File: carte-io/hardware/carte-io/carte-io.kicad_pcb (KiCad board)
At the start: 4 copper layers, 100 x 80 mm, 50 parts, among them J1 USB_C_Receptacle_USB2.0_14P, J2 JST-XH_S2B-XH-A, J3 TSW-104-07-G-T, J4 JST_PH_B4B, J5 TSW-104-07-G-T, J6 FTSH-110-01-L-DV-007, U1 STM32U545VETx, U2 FT231XQ, U3 LT1963AxST-3.3, X1 ASE-16.000MHZ-LC-T

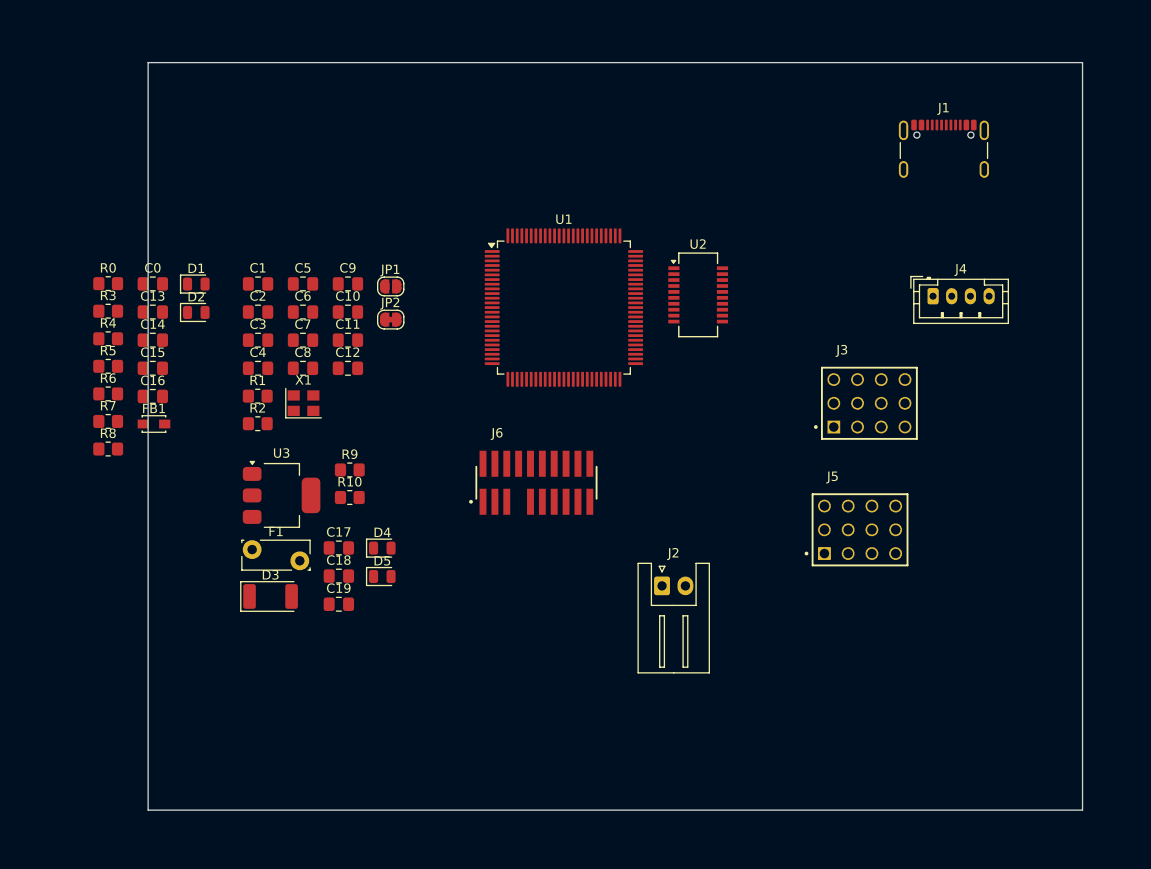
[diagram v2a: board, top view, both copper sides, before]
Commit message: Carte IO routée version 1
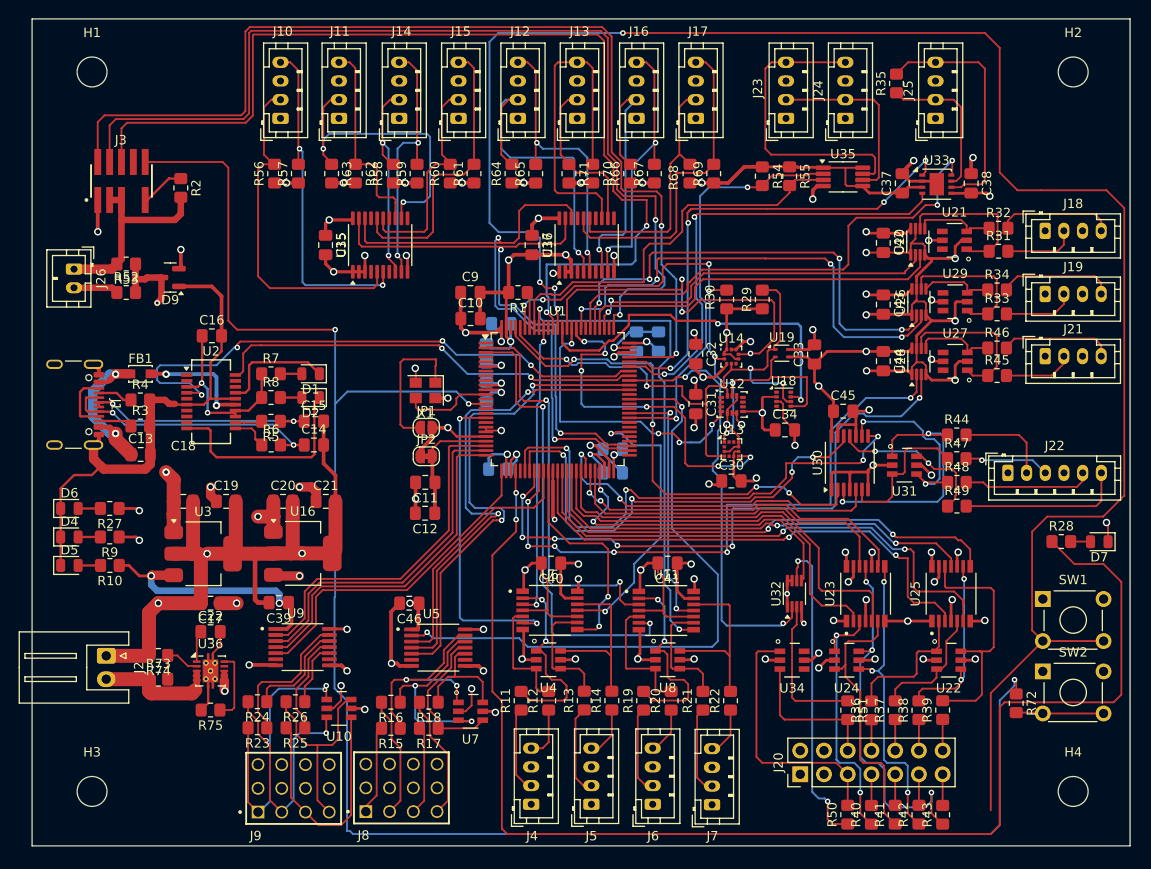
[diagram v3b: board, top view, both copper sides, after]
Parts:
- removed C0: 100nF, Capacitor_SMD:C_0805_2012Metric_Pad1.18x1.45mm_HandSolder
- removed D3: D, Diode_SMD:D_2010_5025Metric
- removed F1: Polyfuse, Fuse:Fuse_Bourns_MF-RG300
- removed R0: 100R, Resistor_SMD:R_0805_2012Metric_Pad1.20x1.40mm_HandSolder
- added C20: 100nF, Capacitor_SMD:C_0805_2012Metric_Pad1.18x1.45mm_HandSolder, F.Cu at (114.4, 107.0)
- added C21: 10µF, Capacitor_SMD:C_0805_2012Metric_Pad1.18x1.45mm_HandSolder, F.Cu at (119.0, 107.0)
- added C22: 100nF, Capacitor_SMD:C_0805_2012Metric_Pad1.18x1.45mm_HandSolder, F.Cu at (106.7, 120.9)
- added C30: 100nF, Capacitor_SMD:C_0805_2012Metric_Pad1.18x1.45mm_HandSolder, F.Cu at (162.4, 104.8)
- added C31: 100nF, Capacitor_SMD:C_0805_2012Metric_Pad1.18x1.45mm_HandSolder, F.Cu at (158.6, 96.5)
- added C32: 100nF, Capacitor_SMD:C_0805_2012Metric_Pad1.18x1.45mm_HandSolder, F.Cu at (158.6, 91.2)
- added C33: 100nF, Capacitor_SMD:C_0805_2012Metric_Pad1.18x1.45mm_HandSolder, F.Cu at (171.3, 91.2)
- added C34: 100nF, Capacitor_SMD:C_0805_2012Metric_Pad1.18x1.45mm_HandSolder, F.Cu at (168.1, 99.3)
- added C35: 100nF, Capacitor_SMD:C_0805_2012Metric_Pad1.18x1.45mm_HandSolder, F.Cu at (119.0, 79.5)
- added C36: 100nF, Capacitor_SMD:C_0805_2012Metric_Pad1.18x1.45mm_HandSolder, F.Cu at (141.1, 79.5)
- added C37: 100nF, Capacitor_SMD:C_0805_2012Metric_Pad1.18x1.45mm_HandSolder, F.Cu at (180.7, 72.9)
- added C38: 100nF, Capacitor_SMD:C_0805_2012Metric_Pad1.18x1.45mm_HandSolder, F.Cu at (188.1, 72.9)
- added C39: 100nF, Capacitor_SMD:C_0805_2012Metric_Pad1.18x1.45mm_HandSolder, F.Cu at (114.0, 117.8)
- added C40: 100nF, Capacitor_SMD:C_0805_2012Metric_Pad1.18x1.45mm_HandSolder, F.Cu at (143.1, 113.6)
- added C41: 100nF, Capacitor_SMD:C_0805_2012Metric_Pad1.18x1.45mm_HandSolder, F.Cu at (155.6, 113.6)
- added C42: 100nF, Capacitor_SMD:C_0805_2012Metric_Pad1.18x1.45mm_HandSolder, F.Cu at (178.7, 79.3)
- added C43: 100nF, Capacitor_SMD:C_0805_2012Metric_Pad1.18x1.45mm_HandSolder, F.Cu at (178.7, 85.9)
- added C44: 100nF, Capacitor_SMD:C_0805_2012Metric_Pad1.18x1.45mm_HandSolder, F.Cu at (178.7, 91.9)
- added C45: 100nF, Capacitor_SMD:C_0805_2012Metric_Pad1.18x1.45mm_HandSolder, F.Cu at (174.4, 97.3)
- added C46: 100nF, Capacitor_SMD:C_0805_2012Metric_Pad1.18x1.45mm_HandSolder, F.Cu at (128.0, 117.9)
- added D6: LED, LED_SMD:LED_0805_2012Metric, F.Cu at (91.6, 107.7)
- added D7: LED, LED_SMD:LED_0805_2012Metric, F.Cu at (201.8, 111.3)
- added D9: BAT54SFILMY, Package_TO_SOT_SMD:SOT-23, F.Cu at (102.4, 83.0)
- added H1: MountingHole, MountingHole:MountingHole_3.2mm_M3, F.Cu at (94.0, 61.0)
- added H2: MountingHole, MountingHole:MountingHole_3.2mm_M3, F.Cu at (199.0, 61.0)
- added H3: MountingHole, MountingHole:MountingHole_3.2mm_M3, F.Cu at (94.0, 138.0)
- added H4: MountingHole, MountingHole:MountingHole_3.2mm_M3, F.Cu at (199.0, 138.0)
- added J10: JST_PH_B4B, Connector_JST:JST_PH_B4B-PH-K_1x04_P2.00mm_Vertical, F.Cu at (114.2, 66.0)
- added J11: JST_PH_B4B, Connector_JST:JST_PH_B4B-PH-K_1x04_P2.00mm_Vertical, F.Cu at (120.4, 66.0)
- added J12: JST_PH_B4B, Connector_JST:JST_PH_B4B-PH-K_1x04_P2.00mm_Vertical, F.Cu at (139.6, 66.0)
- added J13: JST_PH_B4B, Connector_JST:JST_PH_B4B-PH-K_1x04_P2.00mm_Vertical, F.Cu at (145.9, 66.0)
- added J14: JST_PH_B4B, Connector_JST:JST_PH_B4B-PH-K_1x04_P2.00mm_Vertical, F.Cu at (126.9, 66.0)
- added J15: JST_PH_B4B, Connector_JST:JST_PH_B4B-PH-K_1x04_P2.00mm_Vertical, F.Cu at (133.2, 66.0)
- added J16: JST_PH_B4B, Connector_JST:JST_PH_B4B-PH-K_1x04_P2.00mm_Vertical, F.Cu at (152.3, 66.0)
- added J17: JST_PH_B4B, Connector_JST:JST_PH_B4B-PH-K_1x04_P2.00mm_Vertical, F.Cu at (158.6, 66.0)
- added J18: JST_PH_B4B, Connector_JST:JST_PH_B4B-PH-K_1x04_P2.00mm_Vertical, F.Cu at (196.0, 78.0)
- added J19: JST_PH_B4B, Connector_JST:JST_PH_B4B-PH-K_1x04_P2.00mm_Vertical, F.Cu at (196.0, 84.8)
- added J20: Conn_02x08_Odd_Even, Connector_PinHeader_2.54mm:PinHeader_2x07_P2.54mm_Vertical, F.Cu at (169.8, 136.2)
- added J21: JST_PH_B4B, Connector_JST:JST_PH_B4B-PH-K_1x04_P2.00mm_Vertical, F.Cu at (196.0, 91.4)
- added J22: JST_PH_B6B, Connector_JST:JST_PH_B6B-PH-K_1x06_P2.00mm_Vertical, F.Cu at (192.0, 103.9)
- added J23: JST_PH_B4B, Connector_JST:JST_PH_B4B-PH-K_1x04_P2.00mm_Vertical, F.Cu at (168.3, 66.0)
- added J24: JST_PH_B4B, Connector_JST:JST_PH_B4B-PH-K_1x04_P2.00mm_Vertical, F.Cu at (174.6, 66.0)
- added J25: JST_PH_B4B, Connector_JST:JST_PH_B4B-PH-K_1x04_P2.00mm_Vertical, F.Cu at (184.3, 66.0)
- added J26: JST-PH-B2B, Connector_JST:JST_PH_B2B-PH-K_1x02_P2.00mm_Vertical, F.Cu at (92.1, 82.1)
- added J7: JST_PH_B4B, Connector_JST:JST_PH_B4B-PH-K_1x04_P2.00mm_Vertical, F.Cu at (160.3, 139.4)
- added J8: TSW-104-07-G-T, TSW-104-07-G-T:SAMTEC_TSW-104-07-G-T, F.Cu at (127.1, 137.6)
- added J9: TSW-104-07-G-T, TSW-104-07-G-T:SAMTEC_TSW-104-07-G-T, F.Cu at (115.6, 137.7)
- added R11: 100R, Resistor_SMD:R_0805_2012Metric_Pad1.20x1.40mm_HandSolder, F.Cu at (139.9, 128.3)
- added R12: 100R, Resistor_SMD:R_0805_2012Metric_Pad1.20x1.40mm_HandSolder, F.Cu at (142.9, 128.3)
- added R13: 100R, Resistor_SMD:R_0805_2012Metric_Pad1.20x1.40mm_HandSolder, F.Cu at (146.7, 128.3)
- added R14: 100R, Resistor_SMD:R_0805_2012Metric_Pad1.20x1.40mm_HandSolder, F.Cu at (149.6, 128.3)
- added R15: 100R, Resistor_SMD:R_0805_2012Metric_Pad1.20x1.40mm_HandSolder, F.Cu at (126.0, 131.2)
- added R16: 100R, Resistor_SMD:R_0805_2012Metric_Pad1.20x1.40mm_HandSolder, F.Cu at (126.0, 128.5)
- added R17: 100R, Resistor_SMD:R_0805_2012Metric_Pad1.20x1.40mm_HandSolder, F.Cu at (130.0, 131.2)
- added R18: 100R, Resistor_SMD:R_0805_2012Metric_Pad1.20x1.40mm_HandSolder, F.Cu at (130.0, 128.5)
- added R19: 100R, Resistor_SMD:R_0805_2012Metric_Pad1.20x1.40mm_HandSolder, F.Cu at (153.0, 128.3)
- added R20: 100R, Resistor_SMD:R_0805_2012Metric_Pad1.20x1.40mm_HandSolder, F.Cu at (156.0, 128.3)
- added R21: 100R, Resistor_SMD:R_0805_2012Metric_Pad1.20x1.40mm_HandSolder, F.Cu at (159.4, 128.3)
- added R22: 100R, Resistor_SMD:R_0805_2012Metric_Pad1.20x1.40mm_HandSolder, F.Cu at (162.3, 128.3)
- added R23: 100R, Resistor_SMD:R_0805_2012Metric_Pad1.20x1.40mm_HandSolder, F.Cu at (111.7, 131.2)
- added R24: 100R, Resistor_SMD:R_0805_2012Metric_Pad1.20x1.40mm_HandSolder, F.Cu at (111.7, 128.4)
- added R25: 100R, Resistor_SMD:R_0805_2012Metric_Pad1.20x1.40mm_HandSolder, F.Cu at (115.8, 131.2)
- added R26: 100R, Resistor_SMD:R_0805_2012Metric_Pad1.20x1.40mm_HandSolder, F.Cu at (115.8, 128.4)
- added R27: 100R, Resistor_SMD:R_0805_2012Metric_Pad1.20x1.40mm_HandSolder, F.Cu at (95.9, 107.7)
- added R28: 1K, Resistor_SMD:R_0805_2012Metric_Pad1.20x1.40mm_HandSolder, F.Cu at (197.7, 111.3)
- added R29: 1K, Resistor_SMD:R_0805_2012Metric_Pad1.20x1.40mm_HandSolder, F.Cu at (165.7, 85.3)
- added R30: 1K, Resistor_SMD:R_0805_2012Metric_Pad1.20x1.40mm_HandSolder, F.Cu at (161.9, 85.3)
- added R31: 100R, Resistor_SMD:R_0805_2012Metric_Pad1.20x1.40mm_HandSolder, F.Cu at (191.0, 80.2)
- added R32: 100R, Resistor_SMD:R_0805_2012Metric_Pad1.20x1.40mm_HandSolder, F.Cu at (191.0, 77.7)
- added R33: 100R, Resistor_SMD:R_0805_2012Metric_Pad1.20x1.40mm_HandSolder, F.Cu at (190.9, 86.9)
- added R34: 100R, Resistor_SMD:R_0805_2012Metric_Pad1.20x1.40mm_HandSolder, F.Cu at (190.9, 84.3)
- added R35: 120R, Resistor_SMD:R_0805_2012Metric_Pad1.20x1.40mm_HandSolder, F.Cu at (180.1, 62.2)
- added R36: 100R, Resistor_SMD:R_0805_2012Metric_Pad1.20x1.40mm_HandSolder, F.Cu at (177.4, 129.3)
- added R37: 100R, Resistor_SMD:R_0805_2012Metric_Pad1.20x1.40mm_HandSolder, F.Cu at (179.9, 129.3)
- added R38: 100R, Resistor_SMD:R_0805_2012Metric_Pad1.20x1.40mm_HandSolder, F.Cu at (182.5, 129.3)
- added R39: 100R, Resistor_SMD:R_0805_2012Metric_Pad1.20x1.40mm_HandSolder, F.Cu at (185.0, 129.3)
- added R40: 100R, Resistor_SMD:R_0805_2012Metric_Pad1.20x1.40mm_HandSolder, F.Cu at (177.4, 140.5)
- added R41: 100R, Resistor_SMD:R_0805_2012Metric_Pad1.20x1.40mm_HandSolder, F.Cu at (179.9, 140.5)
- added R42: 100R, Resistor_SMD:R_0805_2012Metric_Pad1.20x1.40mm_HandSolder, F.Cu at (182.5, 140.5)
- added R43: 100R, Resistor_SMD:R_0805_2012Metric_Pad1.20x1.40mm_HandSolder, F.Cu at (185.0, 140.5)
- added R44: 100R, Resistor_SMD:R_0805_2012Metric_Pad1.20x1.40mm_HandSolder, F.Cu at (186.5, 99.8)
- added R45: 100R, Resistor_SMD:R_0805_2012Metric_Pad1.20x1.40mm_HandSolder, F.Cu at (190.9, 93.5)
- added R46: 100R, Resistor_SMD:R_0805_2012Metric_Pad1.20x1.40mm_HandSolder, F.Cu at (190.9, 90.5)
- added R47: 100R, Resistor_SMD:R_0805_2012Metric_Pad1.20x1.40mm_HandSolder, F.Cu at (186.5, 102.4)
- added R48: 100R, Resistor_SMD:R_0805_2012Metric_Pad1.20x1.40mm_HandSolder, F.Cu at (186.6, 104.9)
- added R49: 100R, Resistor_SMD:R_0805_2012Metric_Pad1.20x1.40mm_HandSolder, F.Cu at (186.6, 107.5)
- added R50: 100R, Resistor_SMD:R_0805_2012Metric_Pad1.20x1.40mm_HandSolder, F.Cu at (174.9, 140.5)
- added R51: 100R, Resistor_SMD:R_0805_2012Metric_Pad1.20x1.40mm_HandSolder, F.Cu at (174.9, 129.3)
- added R52: 100R, Resistor_SMD:R_0805_2012Metric_Pad1.20x1.40mm_HandSolder, F.Cu at (97.7, 84.6)
- added R53: 100R, Resistor_SMD:R_0805_2012Metric_Pad1.20x1.40mm_HandSolder, F.Cu at (97.7, 81.6)
- added R54: 1K, Resistor_SMD:R_0805_2012Metric_Pad1.20x1.40mm_HandSolder, F.Cu at (165.7, 72.2)
- added R55: 1K, Resistor_SMD:R_0805_2012Metric_Pad1.20x1.40mm_HandSolder, F.Cu at (168.7, 72.2)
- added R56: 1K, Resistor_SMD:R_0805_2012Metric_Pad1.20x1.40mm_HandSolder, F.Cu at (113.5, 71.9)
- added R57: 1K, Resistor_SMD:R_0805_2012Metric_Pad1.20x1.40mm_HandSolder, F.Cu at (116.1, 71.9)
- added R58: 1K, Resistor_SMD:R_0805_2012Metric_Pad1.20x1.40mm_HandSolder, F.Cu at (126.2, 71.9)
- added R59: 1K, Resistor_SMD:R_0805_2012Metric_Pad1.20x1.40mm_HandSolder, F.Cu at (128.8, 71.9)
- added R60: 1K, Resistor_SMD:R_0805_2012Metric_Pad1.20x1.40mm_HandSolder, F.Cu at (132.3, 71.9)
- added R61: 1K, Resistor_SMD:R_0805_2012Metric_Pad1.20x1.40mm_HandSolder, F.Cu at (134.9, 71.9)
- added R62: 1K, Resistor_SMD:R_0805_2012Metric_Pad1.20x1.40mm_HandSolder, F.Cu at (122.2, 71.9)
- added R63: 1K, Resistor_SMD:R_0805_2012Metric_Pad1.20x1.40mm_HandSolder, F.Cu at (119.6, 71.9)
- added R64: 1K, Resistor_SMD:R_0805_2012Metric_Pad1.20x1.40mm_HandSolder, F.Cu at (138.9, 71.9)
- added R65: 1K, Resistor_SMD:R_0805_2012Metric_Pad1.20x1.40mm_HandSolder, F.Cu at (141.5, 71.9)
- added R66: 1K, Resistor_SMD:R_0805_2012Metric_Pad1.20x1.40mm_HandSolder, F.Cu at (151.6, 71.9)
- added R67: 1K, Resistor_SMD:R_0805_2012Metric_Pad1.20x1.40mm_HandSolder, F.Cu at (154.2, 71.9)
- added R68: 1K, Resistor_SMD:R_0805_2012Metric_Pad1.20x1.40mm_HandSolder, F.Cu at (158.0, 71.9)
- added R69: 1K, Resistor_SMD:R_0805_2012Metric_Pad1.20x1.40mm_HandSolder, F.Cu at (160.5, 71.9)
- added R70: 1K, Resistor_SMD:R_0805_2012Metric_Pad1.20x1.40mm_HandSolder, F.Cu at (147.6, 71.9)
- added R71: 1K, Resistor_SMD:R_0805_2012Metric_Pad1.20x1.40mm_HandSolder, F.Cu at (145.0, 71.9)
- added R72: 10K, Resistor_SMD:R_0805_2012Metric_Pad1.20x1.40mm_HandSolder, F.Cu at (192.9, 128.6)
- added R73: 5.1K, Resistor_SMD:R_0805_2012Metric_Pad1.20x1.40mm_HandSolder, F.Cu at (101.1, 126.0)
- added R74: 5.1K, Resistor_SMD:R_0805_2012Metric_Pad1.20x1.40mm_HandSolder, F.Cu at (101.1, 123.4)
- added R75: 5.1K, Resistor_SMD:R_0805_2012Metric_Pad1.20x1.40mm_HandSolder, F.Cu at (106.7, 129.3)
- added SW1: SW_Push, Button_Switch_THT:SW_TH_Tactile_Omron_B3F-10xx, F.Cu at (195.8, 117.4)
- added SW2: SW_Push, Button_Switch_THT:SW_TH_Tactile_Omron_B3F-10xx, F.Cu at (195.8, 125.2)
- added U10: CM1293A-04SO, CM1293A-04SO:SOT95P285X140-6N, F.Cu at (120.4, 129.1)
- added U11: 74LVC125APW, 74LVC125APW:IC_74LVC125APW, F.Cu at (155.4, 118.6)
- added U12: LSM6DS3, Package_LGA:LGA-14_3x2.5mm_P0.5mm_LayoutBorder3x4y, F.Cu at (162.5, 96.6)
- added U13: LIS2MDL, Package_LGA:LGA-12_2x2mm_P0.5mm, F.Cu at (162.4, 101.4)
- added U14: LPS22DF, Package_LGA:ST_HLGA-10_2x2mm_P0.5mm_LayoutBorder3x2y, F.Cu at (162.4, 91.5)
- added U15: PCA9544APW, Package_SO:TSSOP-20_4.4x6.5mm_P0.65mm, F.Cu at (124.8, 79.5)
- added U16: LT1963AxST-3.3, Package_TO_SOT_SMD:SOT-223-3_TabPin2, F.Cu at (116.6, 112.5)
- added U17: PCA9544APW, Package_SO:TSSOP-20_4.4x6.5mm_P0.65mm, F.Cu at (146.9, 79.5)
- added U18: APDS-9251-001, OptoDevice:Broadcom_LGA-8_2x2mm_P0.5mm, F.Cu at (168.0, 96.0)
- added U19: SHT4x, Sensor_Humidity:Sensirion_DFN-4_1.5x1.5mm_P0.8mm_SHT4x_NoCentralPad, F.Cu at (167.8, 91.1)
- added U20: 74LVC2G125DP,125, Package_SO:VSSOP-8_2.3x2mm_P0.5mm, F.Cu at (182.4, 79.2)
- added U21: CM1293A-04SO, CM1293A-04SO:SOT95P285X140-6N, F.Cu at (186.3, 79.0)
- added U22: CM1293A-04SO, CM1293A-04SO:SOT95P285X140-6N, F.Cu at (185.7, 124.0)
- added U23: 74LVC125APW, 74LVC125APW:IC_74LVC125APW, F.Cu at (176.8, 116.8)
- added U24: CM1293A-04SO, CM1293A-04SO:SOT95P285X140-6N, F.Cu at (174.8, 124.0)
- added U25: 74LVC125APW, 74LVC125APW:IC_74LVC125APW, F.Cu at (185.9, 116.8)
- added U26: 74LVC2G125DP,125, Package_SO:VSSOP-8_2.3x2mm_P0.5mm, F.Cu at (182.5, 85.6)
- added U27: CM1293A-04SO, CM1293A-04SO:SOT95P285X140-6N, F.Cu at (186.4, 92.0)
- added U28: 74LVC2G125DP,125, Package_SO:VSSOP-8_2.3x2mm_P0.5mm, F.Cu at (182.5, 92.0)
- added U29: CM1293A-04SO, CM1293A-04SO:SOT95P285X140-6N, F.Cu at (186.4, 85.6)
- added U30: 74LVC125APW,118, Package_SO:TSSOP-14_4.4x5mm_P0.65mm, F.Cu at (175.1, 102.8)
- added U31: CM1293A-04SO, CM1293A-04SO:SOT95P285X140-6N, F.Cu at (180.9, 103.1)
- added U32: 74LVC2G125DP,125, Package_SO:VSSOP-8_2.3x2mm_P0.5mm, F.Cu at (169.2, 116.8)
- added U33: MCP2542FDxMF, Package_DFN_QFN:DFN-8-1EP_3x3mm_P0.65mm_EP1.55x2.4mm, F.Cu at (184.4, 73.0)
- added U34: CM1293A-04SO, CM1293A-04SO:SOT95P285X140-6N, F.Cu at (168.9, 124.0)
- added U35: TCA9802, Package_SO:VSSOP-8_3x3mm_P0.65mm, F.Cu at (174.4, 72.2)
- added U36: TPS259250DRCT, Package_SON:VSON-10-1EP_3x3mm_P0.5mm_EP1.65x2.4mm_ThermalVias, F.Cu at (106.7, 125.1)
- added U4: CM1293A-04SO, CM1293A-04SO:SOT95P285X140-6N, F.Cu at (142.8, 123.9)
- added U5: TXU0104PWR, TXU0104PWR:SOP65P640X120-14N, F.Cu at (131.1, 122.6)
- added U6: 74LVC125APW, 74LVC125APW:IC_74LVC125APW, F.Cu at (143.0, 118.6)
- added U7: CM1293A-04SO, CM1293A-04SO:SOT95P285X140-6N, F.Cu at (134.5, 129.4)
- added U8: CM1293A-04SO, CM1293A-04SO:SOT95P285X140-6N, F.Cu at (155.6, 123.9)
- added U9: TXU0104PWR, TXU0104PWR:SOP65P640X120-14N, F.Cu at (116.5, 122.6)
- C1, C2, C3, C4, C5, C6, C7, C8: moved to B.Cu
- C14: value 10nf -> 47pF
- C16: value 47pF -> 10nf
- C17, C19: value 100nF -> 10µF
- J3: value TSW-104-07-G-T -> FTSH-105-01-L-DV-007; footprint TSW-104-07-G-T:SAMTEC_TSW-104-07-G-T -> FTSH-105-01-L-DV-007-K:SAMTEC_FTSH-105-X-X-DV-007-P-X
- J5: value TSW-104-07-G-T -> JST_PH_B4B; footprint TSW-104-07-G-T:SAMTEC_TSW-104-07-G-T -> Connector_JST:JST_PH_B4B-PH-K_1x04_P2.00mm_Vertical
- J6: value FTSH-110-01-L-DV-007 -> JST_PH_B4B; footprint FTSH-110-01-L-DV-007:SAMTEC_FTSH-110-01-L-DV-007 -> Connector_JST:JST_PH_B4B-PH-K_1x04_P2.00mm_Vertical
- R2: value 100R -> 10K
- R5, R6: value 100R -> 27R
- R7, R8: value 27R -> 1K
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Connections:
- net /CPU/LPUART1_RX renamed /CPU/COM_EXT_RX
- net /CPU/SPI2_MOSI renamed /CPU/US_PulseStart
- net Net-(U2-VCC) renamed /Power & Analog/FT231_VCC
- C14 pad 1: Net-(U2-3V3OUT) -> /Power & Analog/USB-DP
- C15 pad 1: Net-(C15-Pad1) -> /Power & Analog/USB-DN
- C16 pad 1: Net-(C16-Pad1) -> Net-(U2-3V3OUT)
- J1 pad A6: Net-(C16-Pad1) -> /Power & Analog/USB-DN
- J1 pad A7: Net-(C16-Pad1) -> /Power & Analog/USB-DN
- J1 pad B6: Net-(C15-Pad1) -> /Power & Analog/USB-DP
- J1 pad B7: Net-(C15-Pad1) -> /Power & Analog/USB-DP
- J2 pad 2: Net-(J2-Pin_2) -> /Power & Analog/VIN
- J3 pad 01: unconnected-(J3-Pad01) -> +3.3V
- J3 pad 02: unconnected-(J3-Pad02) -> /CPU/JTMS-SWDIO
- J3 pad 03: unconnected-(J3-Pad03) -> GND
- J3 pad 04: unconnected-(J3-Pad04) -> /CPU/JTCK-SWCLK
- J3 pad 05: unconnected-(J3-Pad05) -> GND
- J3 pad 06: unconnected-(J3-Pad06) -> /CPU/JTDO-SWO
- J3 pad 09: unconnected-(J3-Pad09) -> /CPU/GNDDetect
- J3 pad 10: unconnected-(J3-Pad10) -> /CPU/NRST
- J4 pad 1: unconnected-(J4-Pin_1-Pad1) -> +3.3V
- J4 pad 2: unconnected-(J4-Pin_2-Pad2) -> Net-(J4-Pin_2)
- J4 pad 3: unconnected-(J4-Pin_3-Pad3) -> GND
- J4 pad 4: unconnected-(J4-Pin_4-Pad4) -> Net-(J4-Pin_4)
- R5 pad 1: Net-(U2-3V3OUT) -> /Power & Analog/USB-DN
- R5 pad 2: Net-(D1-A) -> /Power & Analog/USB2-DN
- R6 pad 1: Net-(U2-3V3OUT) -> /Power & Analog/USB2-DP
- R6 pad 2: Net-(D2-A) -> /Power & Analog/USB-DP
- R7 pad 1: Net-(C16-Pad1) -> Net-(U2-3V3OUT)
- R7 pad 2: Net-(U2-USBDM) -> Net-(D1-A)
- R8 pad 1: Net-(U2-USBDP) -> Net-(U2-3V3OUT)
- R8 pad 2: Net-(C15-Pad1) -> Net-(D2-A)
- U1 pad 17: /CPU/SPI2_MISO -> /CPU/ENCODER_1_PHB
- U1 pad 29: /CPU/US_PWM -> /CPU/LED_ACTIVITY
- U1 pad 32: /CPU/I2C3_SCL -> /CPU/SPI_MOSI
- U1 pad 36: unconnected-(U1-PB1-Pad36) -> /CPU/ENCODER_2_PHA
- U1 pad 38: unconnected-(U1-PE7-Pad38) -> /CPU/INPUT1
- U1 pad 39: unconnected-(U1-PE8-Pad39) -> /CPU/INPUT2
- U1 pad 4: unconnected-(U1-PE5-Pad4) -> /CPU/~{POWEROFF}
- U1 pad 40: /CPU/ENCODER_1_PHA -> /CPU/INPUT3
- U1 pad 41: unconnected-(U1-PE10-Pad41) -> /CPU/INPUT4
- U1 pad 42: /CPU/ENCODER_1_PHB -> /CPU/OUTPUT1
- U1 pad 43: unconnected-(U1-PE12-Pad43) -> /CPU/OUTPUT2
- U1 pad 45: unconnected-(U1-PE14-Pad45) -> /CPU/OUTPUT3
- U1 pad 46: /CPU/SPI_MOSI -> /CPU/OUTPUT4
- U1 pad 47: /CPU/ENCODER_2_PHB -> /CPU/GEN_PWM2
- U1 pad 52: /CPU/SPI2_SCK -> /CPU/I2C_SCL_EXTERNAL
- U1 pad 53: /CPU/GEN_PWM1 -> /CPU/I2C_SDA_EXTERNAL
- U1 pad 54: /CPU/GEN_PWM2 -> unconnected-(U1-PB15-Pad54)
- U1 pad 56: unconnected-(U1-PD9-Pad56) -> /CPU/ENCODER_2_PHB
- U1 pad 59: /CPU/ENCODER_4_PHA -> /CPU/I2C_SCL_ARBITRARY
- U1 pad 62: unconnected-(U1-PD15-Pad62) -> /CPU/US_PulseEnd
- U1 pad 67: unconnected-(U1-PA8-Pad67) -> /CPU/GEN_PWM1
- U1 pad 77: /CPU/ENCODER_2_PHA -> unconnected-(U1-PA15-Pad77)
- U1 pad 81: unconnected-(U1-PD0-Pad81) -> /CPU/FDCAN_STBY
- U1 pad 84: unconnected-(U1-PD3-Pad84) -> /CPU/INT_MAGNETO
- U1 pad 85: unconnected-(U1-PD4-Pad85) -> /CPU/INT_IMU
- U1 pad 86: unconnected-(U1-PD5-Pad86) -> /CPU/INT_PRESSURE
- U1 pad 87: unconnected-(U1-PD6-Pad87) -> /CPU/INT_LIGHT
- U1 pad 88: unconnected-(U1-PD7-Pad88) -> /CPU/USER_BTN
- U1 pad 90: /CPU/I2C_SDA_EXT -> unconnected-(U1-PB4-Pad90)
- U1 pad 91: unconnected-(U1-PB5-Pad91) -> /CPU/ENCODER_1_PHA
- U1 pad 92: /CPU/I2C_SCL_INT -> /CPU/ENCODER_4_PHA
- U1 pad 93: /CPU/I2C_SDA_EXT -> /CPU/I2C_SDA_ARBITRARY
- U1 pad 95: unconnected-(U1-PB8-Pad95) -> /CPU/I2C_SCL_INT
- U1 pad 96: unconnected-(U1-PB9-Pad96) -> /CPU/I2C_SDA_INT
- U1 pad 97: unconnected-(U1-PE0-Pad97) -> /CPU/SPI_CS
- U2 pad 11: Net-(U2-USBDP) -> /Power & Analog/USB2-DP
- U2 pad 12: Net-(U2-USBDM) -> /Power & Analog/USB2-DN
- U2 pad 20: /IO/USB_UART_TX -> /CPU/COM_USB_TX
- U2 pad 4: /IO/USB_UART_RX -> /CPU/COM_USB_RX
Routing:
- net GND: track 0.00 -> 440.0 mm, vias 0 -> 59
- net +3.3V: track 0.00 -> 319.9 mm, vias 0 -> 53
- net /CPU/USER_BTN: track 0.00 -> 201.6 mm, vias 0 -> 4
- net /CPU/NRST: track 0.00 -> 197.0 mm, vias 0 -> 3
- net +3.3V_PWR: track 0.00 -> 191.5 mm, vias 0 -> 3
- net +5V: track 0.00 -> 180.5 mm, vias 0 -> 9
- net /CPU/LED_ACTIVITY: track 0.00 -> 141.2 mm, vias 0 -> 2
- net /CPU/JTMS-SWDIO: track 0.00 -> 112.9 mm, vias 0 -> 2
- net /CPU/JTDO-SWO: track 0.00 -> 109.0 mm, vias 0 -> 2
- net /CPU/JTCK-SWCLK: track 0.00 -> 106.9 mm, vias 0 -> 2
- net /CPU/ADC_VBAT: track 0.00 -> 76.3 mm, vias 0 -> 2
- net /CPU/SERVO_PWM1: track 0.00 -> 67.3 mm, vias 0 -> 2
- net /CPU/COM_GPS_RX: track 0.00 -> 67.1 mm, vias 0 -> 6
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- added copper zone on In2.Cu, net +3.3V
- added copper zone on In2.Cu, net +3.3V_PWR
- added copper zone on In2.Cu, net +5V
- added copper zone on In1.Cu, net GND
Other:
- board size 100 x 80 mm -> 117.5 x 88.5 mm

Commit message: Correction de DRC et modifications cosmetiques
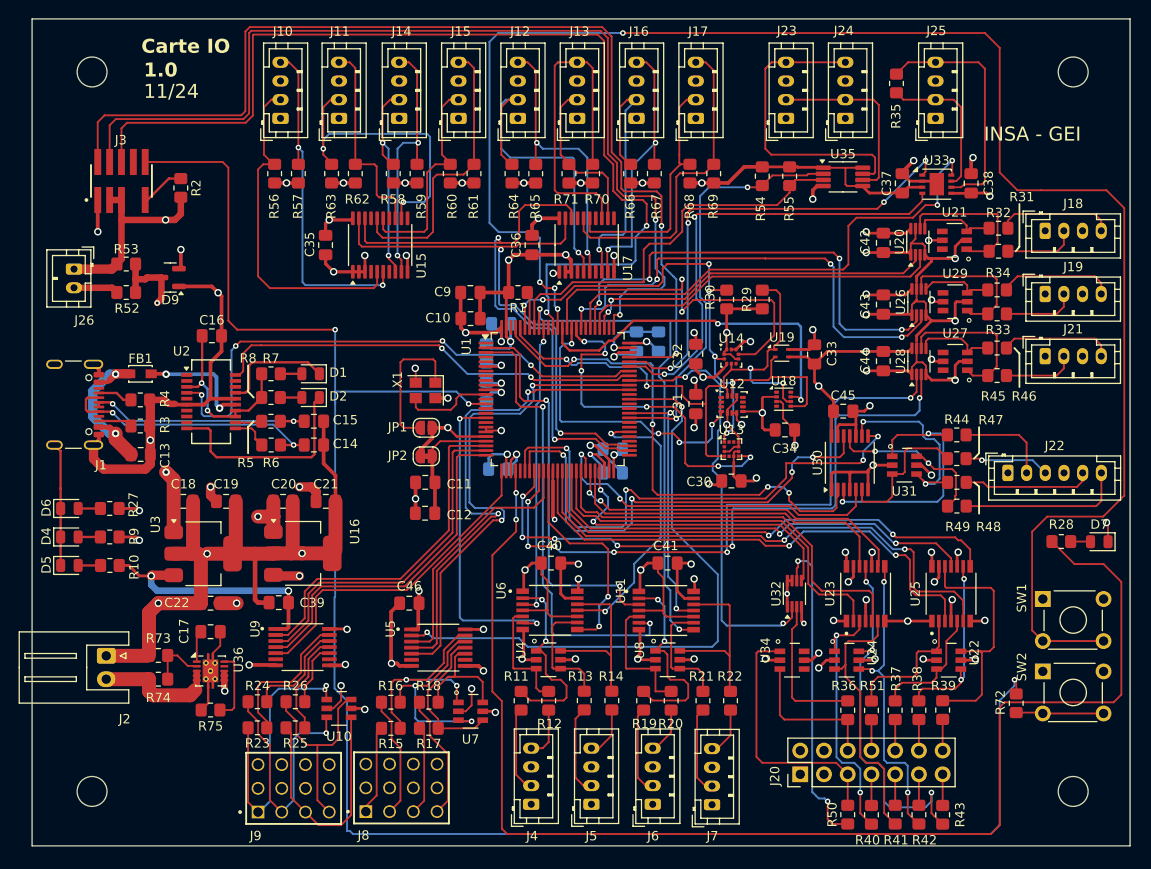
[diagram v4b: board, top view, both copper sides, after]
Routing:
- net /CPU/USER_BTN: track 201.6 -> 181.2 mm
- net (no net): track 6.77 -> 0.00 mm
- net /CPU/COM_USB_RX: track 62.1 -> 58.7 mm
- net +3.3V: track 319.9 -> 322.4 mm
- net /CPU/SPI_CS: track 53.0 -> 54.8 mm
- net /CPU/COM_GPS_RX: track 67.1 -> 68.6 mm
- net /CPU/COM_GPS_TX: track 66.9 -> 68.3 mm
- net /CPU/SPI_MOSI: track 49.9 -> 51.3 mm
- net /CPU/INT_LIGHT: track 39.3 -> 38.2 mm
- net /CPU/COM_LIDAR1_TX: track 39.2 -> 38.2 mm
- net /CPU/COM_LIDAR1_RX: track 40.0 -> 39.2 mm
- net /CPU/INPUT1: track 54.4 -> 55.2 mm
- net /CPU/NRST: track 197.0 -> 197.8 mm
- net /CPU/OUTPUT2: track 44.8 -> 44.1 mm
- net /CPU/GEN_PWM2: track 34.5 -> 33.7 mm
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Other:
- board text added: "1.0"
- board text added: "11/24"
- board text added: "Carte IO"
- board text added: "INSA - GEI"

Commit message: Correction du 5V sur les UART (Lidar et GPS + Changement de conencteur J27 (GPS) pour rajouter le 5V et le 3V pour les IO
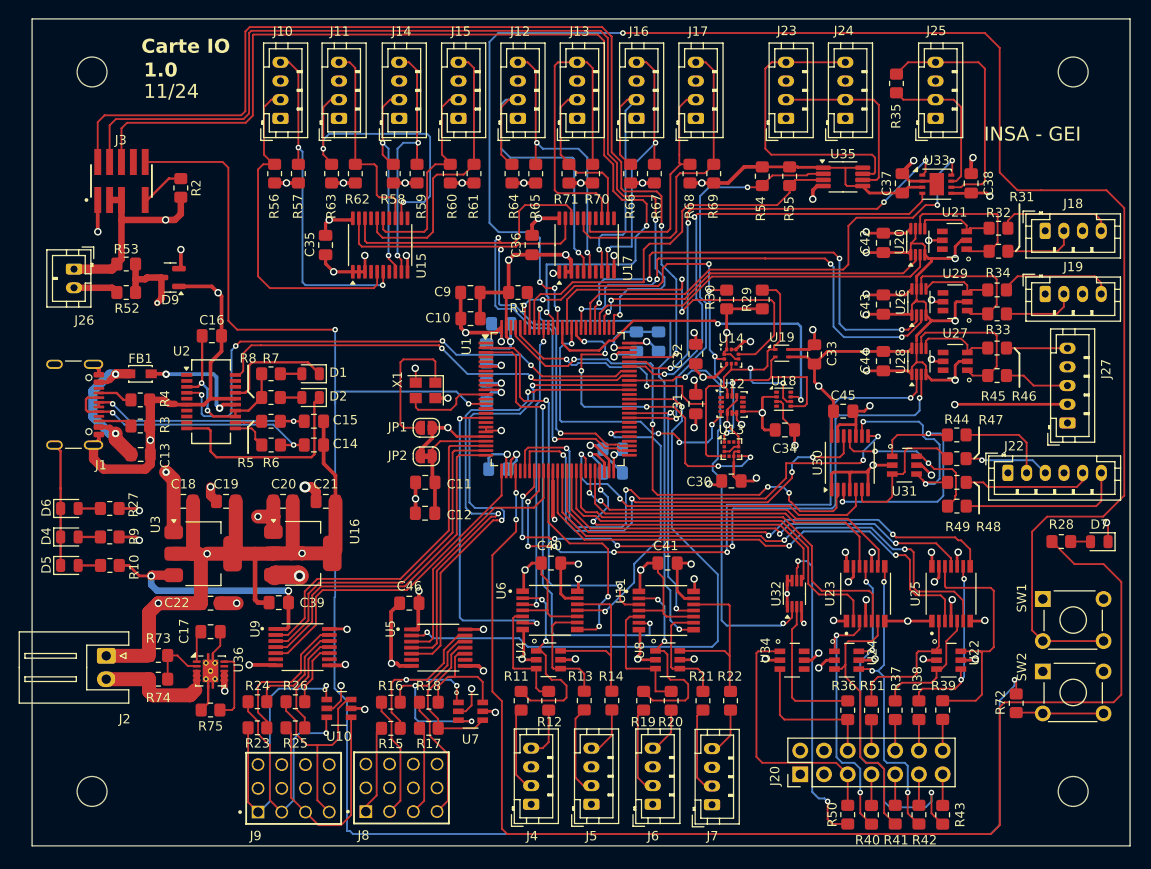
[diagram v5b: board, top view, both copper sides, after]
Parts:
- removed J21: JST_PH_B4B, Connector_JST:JST_PH_B4B-PH-K_1x04_P2.00mm_Vertical
- added J27: JST_PH_B5B, Connector_JST:JST_PH_B5B-PH-K_1x05_P2.00mm_Vertical, F.Cu at (198.4, 98.6)
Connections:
- J18 pad 1: +3.3V_PWR -> +5V
- J19 pad 1: +3.3V_PWR -> +5V
- U21 pad 5: +3.3V -> +5V
- U27 pad 5: +3.3V -> +5V
- U29 pad 5: +3.3V -> +5V
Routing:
- net +5V: track 180.5 -> 225.4 mm, vias 9 -> 12
- net +3.3V: track 322.4 -> 330.3 mm, vias 53 -> 51
- net Net-(J27-Pin_5): track 12.1 -> 6.69 mm
- net Net-(J27-Pin_3): track 7.77 -> 6.98 mm

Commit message: Carte version 1.1 terminée
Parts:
- removed C17: 10µF, Capacitor_SMD:C_0805_2012Metric_Pad1.18x1.45mm_HandSolder
- removed C22, C39, C40, C41, C46: 100nF, Capacitor_SMD:C_0805_2012Metric_Pad1.18x1.45mm_HandSolder
- removed R38, R39, R44, R47, R48, R49, R50, R51: 100R, Resistor_SMD:R_0805_2012Metric_Pad1.20x1.40mm_HandSolder
- removed R75: 5.1K, Resistor_SMD:R_0805_2012Metric_Pad1.20x1.40mm_HandSolder
- removed U22, U31, U34: CM1293A-04SO, CM1293A-04SO:SOT95P285X140-6N
- removed U23, U25: 74LVC125APW, 74LVC125APW:IC_74LVC125APW
- removed U30: 74LVC125APW,118, Package_SO:TSSOP-14_4.4x5mm_P0.65mm
- removed U32: 74LVC2G125DP,125, Package_SO:VSSOP-8_2.3x2mm_P0.5mm
- removed U36: TPS259250DRCT, Package_SON:VSON-10-1EP_3x3mm_P0.5mm_EP1.65x2.4mm_ThermalVias
- added D3: BAT54SFILMY, Package_TO_SOT_SMD:SOT-23, F.Cu at (185.7, 108.7)
- added D8: BAT54SFILMY, Package_TO_SOT_SMD:SOT-23, B.Cu at (185.7, 102.6)
- added J21: 114020164, SeeedStudio - Horizontal Header -114020164:SEEEDSTUDIO_114020164, B.Cu at (172.4, 138.2)
- added J28: 114020164, SeeedStudio - Horizontal Header -114020164:SEEEDSTUDIO_114020164, B.Cu at (185.4, 138.2)
- added J29: 114020164, SeeedStudio - Horizontal Header -114020164:SEEEDSTUDIO_114020164, F.Cu at (199.3, 105.5)
- added J30: 114020164, SeeedStudio - Horizontal Header -114020164:SEEEDSTUDIO_114020164, B.Cu at (199.3, 105.5)
- added JP3: Jumper_2_Bridged, Connector_PinHeader_2.54mm:PinHeader_1x02_P2.54mm_Horizontal, F.Cu at (105.4, 133.5)
- added Q1: IRF9388TRPBF, Package_SO:SOIC-8_3.9x4.9mm_P1.27mm, F.Cu at (103.8, 122.0)
- added R76: 4.7K, Resistor_SMD:R_0805_2012Metric_Pad1.20x1.40mm_HandSolder, F.Cu at (134.2, 78.1)
- added R77: 4.7K, Resistor_SMD:R_0805_2012Metric_Pad1.20x1.40mm_HandSolder, F.Cu at (134.2, 81.0)
- C1: moved to F.Cu
- C33, D9, R13, R14, R21, R22, R37, R41, R42, R52, R53: moved to B.Cu
- J10, J16, J18, J23, J25, J4, J6: value JST_PH_B4B -> 114020164; footprint Connector_JST:JST_PH_B4B-PH-K_1x04_P2.00mm_Vertical -> SeeedStudio - Horizontal Header -114020164:SEEEDSTUDIO_114020164
- J11, J17, J19, J24, J5, J7: value JST_PH_B4B -> 114020164; footprint Connector_JST:JST_PH_B4B-PH-K_1x04_P2.00mm_Vertical -> SeeedStudio - Horizontal Header -114020164:SEEEDSTUDIO_114020164; moved to B.Cu
- J12: renamed from J14; value JST_PH_B4B -> 114020164; footprint Connector_JST:JST_PH_B4B-PH-K_1x04_P2.00mm_Vertical -> SeeedStudio - Horizontal Header -114020164:SEEEDSTUDIO_114020164
- J13: renamed from J15; value JST_PH_B4B -> 114020164; footprint Connector_JST:JST_PH_B4B-PH-K_1x04_P2.00mm_Vertical -> SeeedStudio - Horizontal Header -114020164:SEEEDSTUDIO_114020164; moved to B.Cu
- J14: renamed from J12; value JST_PH_B4B -> 114020164; footprint Connector_JST:JST_PH_B4B-PH-K_1x04_P2.00mm_Vertical -> SeeedStudio - Horizontal Header -114020164:SEEEDSTUDIO_114020164
- J15: renamed from J13; value JST_PH_B4B -> 114020164; footprint Connector_JST:JST_PH_B4B-PH-K_1x04_P2.00mm_Vertical -> SeeedStudio - Horizontal Header -114020164:SEEEDSTUDIO_114020164; moved to B.Cu
- J2: value JST-XH_S2B-XH-A -> 114020164; footprint Connector_JST:JST_XH_S2B-XH-A_1x02_P2.50mm_Horizontal -> SeeedStudio - Horizontal Header -114020164:SEEEDSTUDIO_114020164
- J20: value Conn_02x08_Odd_Even -> 114020164; footprint Connector_PinHeader_2.54mm:PinHeader_2x07_P2.54mm_Vertical -> SeeedStudio - Horizontal Header -114020164:SEEEDSTUDIO_114020164
- J22: value JST_PH_B6B -> 114020164; footprint Connector_JST:JST_PH_B6B-PH-K_1x06_P2.00mm_Vertical -> SeeedStudio - Horizontal Header -114020164:SEEEDSTUDIO_114020164
- J26: value JST-PH-B2B -> 114020164; footprint Connector_JST:JST_PH_B2B-PH-K_1x02_P2.00mm_Vertical -> SeeedStudio - Horizontal Header -114020164:SEEEDSTUDIO_114020164; moved to B.Cu
- J27: value JST_PH_B5B -> 114020164; footprint Connector_JST:JST_PH_B5B-PH-K_1x05_P2.00mm_Vertical -> SeeedStudio - Horizontal Header -114020164:SEEEDSTUDIO_114020164
- J3: value FTSH-105-01-L-DV-007 -> FTSH-105-01-L-DH; footprint FTSH-105-01-L-DV-007-K:SAMTEC_FTSH-105-X-X-DV-007-P-X -> FTSH-105-01-L-DH:SAMTEC_FTSH-105-01-L-DH
- R10, R27: value 100R -> 150R
- R28: value 1K -> 270R
- R29, R30, R54, R55, R56, R57, R58, R59, R64, R65, R66, R67: value 1K -> 4.7K
- R60, R61, R62, R63, R68, R69, R70, R71: value 1K -> 4.7K; moved to B.Cu
- R7, R8: value 1K -> 150R
- R73, R74: value 5.1K -> 4.7K
- R9: value 100R -> 330R
- SW1, SW2: footprint Button_Switch_THT:SW_TH_Tactile_Omron_B3F-10xx -> Button_Switch_SMD:Panasonic_EVQPUJ_EVQPUA
- U20, U26, U28: footprint Package_SO:VSSOP-8_2.3x2mm_P0.5mm -> Package_SO:TSSOP-8_3x3mm_P0.65mm
- moved D7 110.5 mm to (91.4, 105.8), turned to 0 degrees
- moved R28 102.0 mm to (95.8, 105.8), turned to 180 degrees
- moved R73 94.2 mm to (175.8, 68.7), turned to 180 degrees
- moved R74 89.4 mm to (171.7, 68.7), turned to 0 degrees
- moved U18 79.0 mm to (90.1, 82.9)
- moved C34 78.8 mm to (90.4, 86.4), turned to 180 degrees
- moved U19 70.6 mm to (97.7, 82.9), turned to 180 degrees
- moved C33 69.0 mm to (102.8, 82.9), turned to -90 degrees
- moved J26 42.1 mm to (93.3, 124.2), turned to 90 degrees
- moved J22 34.9 mm to (185.4, 138.2)
- moved R53 33.0 mm to (92.0, 114.1), turned to -90 degrees
- moved R52 29.7 mm to (94.2, 114.1), turned to 90 degrees
- moved R37 28.4 mm to (189.8, 102.6), turned to 180 degrees
- moved D9 27.7 mm to (93.2, 109.1), turned to -90 degrees
- moved R36 24.1 mm to (189.8, 108.7), turned to 180 degrees
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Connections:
- J1 pad A6: /Power & Analog/USB-DN -> /Power & Analog/USB-DP
- J1 pad B7: /Power & Analog/USB-DP -> /Power & Analog/USB-DN
- J10 pad 1: +3.3V_PWR -> Net-(J10-Pin_1)
- J10 pad 3: GND -> +3.3V_PWR
- J10 pad 4: Net-(J10-Pin_4) -> GND
- J11 pad 1: +3.3V_PWR -> Net-(J11-Pin_1)
- J11 pad 3: GND -> +3.3V_PWR
- J11 pad 4: Net-(J11-Pin_4) -> GND
- J12 pad 1: +3.3V_PWR -> Net-(J12-Pin_1)
- J12 pad 3: GND -> +3.3V_PWR
- J12 pad 4: Net-(J14-Pin_4) -> GND
- J13 pad 1: +3.3V_PWR -> Net-(J13-Pin_1)
- J13 pad 3: GND -> +3.3V_PWR
- J13 pad 4: Net-(J15-Pin_4) -> GND
- J14 pad 1: +3.3V_PWR -> Net-(J14-Pin_1)
- J14 pad 3: GND -> +3.3V_PWR
- J14 pad 4: Net-(J12-Pin_4) -> GND
- J15 pad 1: +3.3V_PWR -> Net-(J15-Pin_1)
- J15 pad 3: GND -> +3.3V_PWR
- J15 pad 4: Net-(J13-Pin_4) -> GND
- J16 pad 1: +3.3V_PWR -> Net-(J16-Pin_1)
- J16 pad 3: GND -> +3.3V_PWR
- J16 pad 4: Net-(J16-Pin_4) -> GND
- J17 pad 1: +3.3V_PWR -> Net-(J17-Pin_1)
- J17 pad 3: GND -> +3.3V_PWR
- J17 pad 4: Net-(J17-Pin_4) -> GND
- J18 pad 1: +5V -> Net-(J18-Pin_1)
- J18 pad 3: GND -> +5V
- J18 pad 4: Net-(J18-Pin_4) -> GND
- J19 pad 1: +5V -> Net-(J19-Pin_1)
- J19 pad 3: GND -> +5V
- J19 pad 4: Net-(J19-Pin_4) -> GND
- J20 pad 1: +3.3V_PWR -> /GPIO SPI GEN_PWM/IO1
- J20 pad 2: +5V -> unconnected-(J20-Pin_2-Pad2)
- J20 pad 3: GND -> +3.3V
- J22 pad 1: +3.3V_PWR -> /GPIO SPI GEN_PWM/IO4
- J22 pad 2: /GPIO SPI GEN_PWM/SPI_CS_EXT -> unconnected-(J22-Pin_2-Pad2)
- J22 pad 3: /GPIO SPI GEN_PWM/SPI_CLK_EXT -> +3.3V
- J23 pad 1: +3.3V_PWR -> Net-(J23-Pin_1)
- J23 pad 3: GND -> +3.3V_PWR
- J23 pad 4: Net-(J23-Pin_4) -> GND
- J24 pad 1: +3.3V_PWR -> Net-(J23-Pin_1)
- J24 pad 3: GND -> +3.3V_PWR
- J24 pad 4: Net-(J23-Pin_4) -> GND
- J25 pad 1: +5V -> Net-(J25-Pin_1)
- J25 pad 3: GND -> +5V
- J25 pad 4: Net-(J25-Pin_4) -> GND
- J26 pad 1: GND -> /CPU/~{POWEROFF}
- J26 pad 2: Net-(J26-Pin_2) -> /CPU/PWR_CSLEEP
- J27 pad 1: +5V -> Net-(J27-Pin_1)
- J27 pad 2: +3.3V -> Net-(J27-Pin_2)
- J27 pad 3: Net-(J27-Pin_3) -> +5V
- J4 pad 1: +3.3V -> Net-(J4-Pin_1)
- J4 pad 3: GND -> +3.3V
- J4 pad 4: Net-(J4-Pin_4) -> GND
- J5 pad 1: +3.3V -> Net-(J5-Pin_1)
- J5 pad 3: GND -> +3.3V
- J5 pad 4: Net-(J5-Pin_4) -> GND
- J6 pad 1: +3.3V -> Net-(J6-Pin_1)
- J6 pad 3: GND -> +3.3V
- J6 pad 4: Net-(J6-Pin_4) -> GND
- J7 pad 1: +3.3V -> Net-(J7-Pin_1)
- J7 pad 3: GND -> +3.3V
- J7 pad 4: Net-(J7-Pin_4) -> GND
- R11 pad 1: Net-(J4-Pin_2) -> Net-(J4-Pin_1)
- R12 pad 1: Net-(J4-Pin_4) -> Net-(J4-Pin_2)
- R13 pad 1: Net-(J5-Pin_2) -> Net-(J5-Pin_1)
- R14 pad 1: Net-(J5-Pin_4) -> Net-(J5-Pin_2)
- R19 pad 1: Net-(J6-Pin_2) -> Net-(J6-Pin_1)
- R20 pad 1: Net-(J6-Pin_4) -> Net-(J6-Pin_2)
- R21 pad 1: Net-(J7-Pin_2) -> Net-(J7-Pin_1)
- R22 pad 1: Net-(J7-Pin_4) -> Net-(J7-Pin_2)
- R32 pad 2: Net-(J18-Pin_4) -> Net-(J18-Pin_1)
- R34 pad 2: Net-(J19-Pin_4) -> Net-(J19-Pin_1)
- R35 pad 2: Net-(J25-Pin_4) -> Net-(J25-Pin_1)
- R36 pad 1: /GPIO SPI GEN_PWM/IN1 -> /GPIO SPI GEN_PWM/AN1
- R36 pad 2: Net-(U22-CH1) -> /CPU/ADC_AN1
- R37 pad 1: /GPIO SPI GEN_PWM/IN2 -> Net-(J30-Pin_1)
- R37 pad 2: Net-(U22-CH2) -> /CPU/ADC_AN2
- R40 pad 1: Net-(U23-1Y) -> /CPU/IO1
- R40 pad 2: /GPIO SPI GEN_PWM/OUT1 -> /GPIO SPI GEN_PWM/IO1
- R41 pad 1: Net-(U23-2Y) -> /CPU/IO2
- R41 pad 2: /GPIO SPI GEN_PWM/OUT2 -> /GPIO SPI GEN_PWM/IO2
- R42 pad 1: Net-(U23-3Y) -> /CPU/IO3
- R42 pad 2: /GPIO SPI GEN_PWM/OUT3 -> /GPIO SPI GEN_PWM/IO3
- R43 pad 1: Net-(U23-4Y) -> /CPU/IO4
- R43 pad 2: /GPIO SPI GEN_PWM/OUT4 -> /GPIO SPI GEN_PWM/IO4
- R45 pad 2: Net-(J27-Pin_3) -> Net-(J27-Pin_2)
- R46 pad 2: Net-(J27-Pin_5) -> Net-(J27-Pin_1)
- R52 pad 1: Net-(J26-Pin_2) -> Net-(J26-Pin_3)
- R57 pad 2: Net-(J10-Pin_4) -> Net-(J10-Pin_1)
- R59 pad 2: Net-(J14-Pin_4) -> Net-(J12-Pin_1)
- R61 pad 2: Net-(J15-Pin_4) -> Net-(J13-Pin_1)
- R62 pad 1: Net-(J11-Pin_4) -> Net-(J11-Pin_1)
- R65 pad 2: Net-(J12-Pin_4) -> Net-(J14-Pin_1)
- R67 pad 2: Net-(J16-Pin_4) -> Net-(J16-Pin_1)
- R69 pad 2: Net-(J17-Pin_4) -> Net-(J17-Pin_1)
- R70 pad 1: Net-(J13-Pin_4) -> Net-(J15-Pin_1)
- R73 pad 1: /Power & Analog/VIN -> +3.3V
- R73 pad 2: Net-(U36-EN/UVLO) -> Net-(J23-Pin_1)
- R74 pad 1: Net-(U36-EN/UVLO) -> +3.3V
- R74 pad 2: GND -> Net-(J23-Pin_2)
- U1 pad 31: /CPU/SPI_MISO -> unconnected-(U1-PA6-Pad31)
- U1 pad 32: /CPU/SPI_MOSI -> unconnected-(U1-PA7-Pad32)
- U1 pad 38: /CPU/INPUT1 -> /CPU/IO1
- U1 pad 39: /CPU/INPUT2 -> /CPU/IO2
- U1 pad 40: /CPU/INPUT3 -> /CPU/IO3
- U1 pad 41: /CPU/INPUT4 -> /CPU/IO4
- U1 pad 42: /CPU/OUTPUT1 -> unconnected-(U1-PE11-Pad42)
- U1 pad 43: /CPU/OUTPUT2 -> /CPU/ADC_AN1
- U1 pad 44: /CPU/SPI_SCK -> /CPU/ADC_AN2
- U1 pad 45: /CPU/OUTPUT3 -> unconnected-(U1-PE14-Pad45)
- U1 pad 46: /CPU/OUTPUT4 -> unconnected-(U1-PE15-Pad46)
- U1 pad 47: /CPU/GEN_PWM2 -> unconnected-(U1-PB10-Pad47)
- U1 pad 67: /CPU/GEN_PWM1 -> unconnected-(U1-PA8-Pad67)
- U1 pad 97: /CPU/SPI_CS -> unconnected-(U1-PE0-Pad97)
- U15 pad 13: Net-(J11-Pin_4) -> Net-(J11-Pin_1)
- U15 pad 16: Net-(J15-Pin_4) -> Net-(J13-Pin_1)
- U15 pad 6: Net-(J10-Pin_4) -> Net-(J10-Pin_1)
- U15 pad 9: Net-(J14-Pin_4) -> Net-(J12-Pin_1)
- U17 pad 13: Net-(J13-Pin_4) -> Net-(J15-Pin_1)
- U17 pad 16: Net-(J17-Pin_4) -> Net-(J17-Pin_1)
- U17 pad 6: Net-(J12-Pin_4) -> Net-(J14-Pin_1)
- U17 pad 9: Net-(J16-Pin_4) -> Net-(J16-Pin_1)
- U21 pad 5: +5V -> +3.3V
- U24 pad 1: Net-(U23-1Y) -> /CPU/IO1
- U24 pad 3: Net-(U23-2Y) -> /CPU/IO2
- U24 pad 4: Net-(U23-3Y) -> /CPU/IO3
- U24 pad 6: Net-(U23-4Y) -> /CPU/IO4
- U27 pad 5: +5V -> +3.3V
- U29 pad 5: +5V -> +3.3V
- U33 pad 6: Net-(J25-Pin_4) -> Net-(J25-Pin_1)
- U35 pad 7: Net-(J23-Pin_4) -> Net-(J23-Pin_1)
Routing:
- net GND: track 440.5 -> 556.9 mm, vias 62 -> 78
- net /CPU/LED_ACTIVITY: track 141.2 -> 49.7 mm, vias 2 -> 6
- net /CPU/USER_BTN: track 181.2 -> 95.4 mm
- net /CPU/~{POWEROFF}: track 0.00 -> 83.3 mm, vias 0 -> 3
- net /CPU/I2C_SCL_INT: track 65.7 -> 137.7 mm, vias 7 -> 8
- net /CPU/I2C_SDA_INT: track 63.1 -> 132.4 mm, vias 4 -> 5
- net +3.3V: track 330.3 -> 398.7 mm, vias 51 -> 52
- net /CPU/IO2: track 0.00 -> 67.2 mm, vias 0 -> 2
- net +3.3V_PWR: track 191.9 -> 126.8 mm, vias 3 -> 8
- net /CPU/IO3: track 0.00 -> 63.4 mm, vias 0 -> 2
- net /CPU/IO4: track 0.00 -> 61.2 mm
- net /CPU/PWR_CSLEEP: track 0.00 -> 61.0 mm, vias 0 -> 5
- net /CPU/SPI_MISO: track 57.4 -> 0.00 mm, vias 4 -> 0
- net /CPU/INPUT2: track 56.9 -> 0.00 mm, vias 2 -> 0
- net /CPU/IO1: track 0.00 -> 56.6 mm
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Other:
- outline, holes or cut-outs redrawn
- board text added: "${COMPANY}"
- board text added: "${ISSUE_DATE}"
- board text added: "${TITLE} ${REVISION}"
- board text removed: "1.0"
- board text removed: "11/24"
- board text removed: "Carte IO"
- board text removed: "INSA - GEI"
